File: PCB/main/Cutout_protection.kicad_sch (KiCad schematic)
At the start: 0 parts

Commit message: cutout
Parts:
- added D?: DIODE, symbol Simulation_SPICE:DIODE
- added D?: ZMM4V7-M, symbol Device:D_Zener
- added K?: ADW11, Relay_THT:Relay_1P1T_NO_10x24x18.8mm_Panasonic_ADW11xxxxW_THT, symbol Relay:ADW11
- added Q?: 2N3904, Package_TO_SOT_THT:TO-92_Inline, symbol Transistor_BJT:2N3904
- added R?: 150, symbol Device:R
- added R?: 1k, symbol Device:R
- added R?: 100k, symbol Device:R
- added U?: OPAMP, symbol pspice:OPAMP
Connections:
- net Battery_INP: now also D?.2 (K), K?.1, R?.1, R?.1, U?.4 (V+)
- net Relay_INP: now also K?.3
- net Relay_OUT: now also K?.5
- new net: D?.1 (A), K?.6, Q?.3 (C)
- new net: D?.1 (K), R?.2, U?.2 (-)
- new net: Q?.2 (B), U?.3
- new net: R?.1, R?.2, U?.1 (+)
- new net GND: D?.2 (A), Q?.1 (E), R?.2, U?.5 (V-)

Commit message: pmosfet name
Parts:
- gave numbers to parts that had none: 8
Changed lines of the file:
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@@
   (symbol (lib_id "Simulation_SPICE:DIODE") (at 130.81 93.98 90) (unit 1)
     (in_bom yes) (on_board yes) (fields_autoplaced)
-    (property "Reference" "D?" (id 0) (at 133.35 92.7099 90)
+    (property "Reference" "D5" (id 0) (at 133.35 92.7099 90)
       (effects (font (size 1.27 1.27)) (justify right))
     )
@@
   (symbol (lib_id "Device:R") (at 59.69 93.98 0) (unit 1)
     (in_bom yes) (on_board yes) (fields_autoplaced)
-    (property "Reference" "R?" (id 0) (at 62.23 92.7099 0)
+    (property "Reference" "R3" (id 0) (at 62.23 92.7099 0)
       (effects (font (size 1.27 1.27)) (justify left))
     )
@@
   (symbol (lib_id "Transistor_BJT:2N3904") (at 128.27 110.49 0) (unit 1)
     (in_bom yes) (on_board yes) (fields_autoplaced)
-    (property "Reference" "Q?" (id 0) (at 133.35 109.2199 0)
+    (property "Reference" "Q3" (id 0) (at 133.35 109.2199 0)
       (effects (font (size 1.27 1.27)) (justify left))
     )
@@
   (symbol (lib_id "power:GND") (at 54.61 127 0) (unit 1)
     (in_bom yes) (on_board yes) (fields_autoplaced)
-    (property "Reference" "#PWR?" (id 0) (at 54.61 133.35 0)
+    (property "Reference" "#PWR018" (id 0) (at 54.61 133.35 0)
       (effects (font (size 1.27 1.27)) hide)
     )
@@
   (symbol (lib_id "Device:R") (at 82.55 93.98 0) (unit 1)
     (in_bom yes) (on_board yes) (fields_autoplaced)
-    (property "Reference" "R?" (id 0) (at 85.09 92.7099 0)
+    (property "Reference" "R4" (id 0) (at 85.09 92.7099 0)
       (effects (font (size 1.27 1.27)) (justify left))
     )
@@
   (symbol (lib_id "Device:R") (at 82.55 111.76 0) (unit 1)
     (in_bom yes) (on_board yes) (fields_autoplaced)
-    (property "Reference" "R?" (id 0) (at 85.09 110.4899 0)
+    (property "Reference" "R5" (id 0) (at 85.09 110.4899 0)
       (effects (font (size 1.27 1.27)) (justify left))
     )
@@
   (symbol (lib_id "pspice:OPAMP") (at 106.68 101.6 0) (unit 1)
     (in_bom yes) (on_board yes) (fields_autoplaced)
-    (property "Reference" "U?" (id 0) (at 116.84 96.901 0))
+    (property "Reference" "U2" (id 0) (at 116.84 96.901 0))
     (property "Value" "OPAMP" (id 1) (at 116.84 99.441 0))
     (property "Footprint" "" (id 2) (at 106.68 101.6 0)
@@
   (symbol (lib_id "Relay:ADW11") (at 154.94 93.98 0) (unit 1)
     (in_bom yes) (on_board yes) (fields_autoplaced)
-    (property "Reference" "K?" (id 0) (at 166.37 92.7099 0)
+    (property "Reference" "K1" (id 0) (at 166.37 92.7099 0)
       (effects (font (size 1.27 1.27)) (justify left))
     )
@@
   (symbol (lib_id "Device:D_Zener") (at 59.69 111.76 270) (unit 1)
     (in_bom yes) (on_board yes) (fields_autoplaced)
-    (property "Reference" "D?" (id 0) (at 62.23 110.4899 90)
+    (property "Reference" "D4" (id 0) (at 62.23 110.4899 90)
       (effects (font (size 1.27 1.27)) (justify left))
     )

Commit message: Updated BOM
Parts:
- D4: footprint (none) -> Footprint_EEE3088F:LL-34_L3.5-W1.5-RD; JLC Part # (none) -> C707193; Price (none) -> 0.0159
- K1: JLC Part # (none) -> C34758; Price (none) -> 0.5145
- Q3: footprint Package_TO_SOT_THT:TO-92_Inline -> Package_TO_SOT_SMD:SOT-23; JLC Part # (none) -> C20526; Price (none) -> 0.0153
- R3: footprint (none) -> Resistor_SMD:R_0402_1005Metric; JLC Part # (none) -> C25082; Price (none) -> 0.0007
- R4: footprint (none) -> Resistor_SMD:R_0402_1005Metric; JLC Part # (none) -> C11702; Price (none) -> 0.0008
- R5: footprint (none) -> Resistor_SMD:R_0402_1005Metric; JLC Part # (none) -> C25744; Price (none) -> 0.0007
- U2: value OPAMP -> LM358DR2G; footprint (none) -> Package_SO:SOIC-8_3.9x4.9mm_P1.27mm; JLC Part # (none) -> C7950; Price (none) -> 0.149
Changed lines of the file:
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@@
       (effects (font (size 1.27 1.27)) (justify left))
     )
-    (property "Footprint" "" (id 2) (at 57.912 93.98 90)
+    (property "Footprint" "Resistor_SMD:R_0402_1005Metric" (id 2) (at 57.912 93.98 90)
       (effects (font (size 1.27 1.27)) hide)
     )
     (property "Datasheet" "~" (id 3) (at 59.69 93.98 0)
+      (effects (font (size 1.27 1.27)) hide)
+    )
+    (property "JLC Part #" "C25082" (id 4) (at 59.69 93.98 0)
+      (effects (font (size 1.27 1.27)) hide)
+    )
+    (property "Price" "0.0007" (id 5) (at 59.69 93.98 0)
       (effects (font (size 1.27 1.27)) hide)
     )
@@
       (effects (font (size 1.27 1.27)) (justify left))
     )
-    (property "Footprint" "Package_TO_SOT_THT:TO-92_Inline" (id 2) (at 133.35 112.395 0)
+    (property "Footprint" "Package_TO_SOT_SMD:SOT-23" (id 2) (at 133.35 112.395 0)
       (effects (font (size 1.27 1.27) italic) (justify left) hide)
     )
     (property "Datasheet" "https://www.onsemi.com/pub/Collateral/2N3903-D.PDF" (id 3) (at 128.27 110.49 0)
       (effects (font (size 1.27 1.27)) (justify left) hide)
+    )
+    (property "JLC Part #" "C20526" (id 4) (at 128.27 110.49 0)
+      (effects (font (size 1.27 1.27)) hide)
+    )
+    (property "Price" "0.0153" (id 5) (at 128.27 110.49 0)
+      (effects (font (size 1.27 1.27)) hide)
     )
     (pin "1")
@@
       (effects (font (size 1.27 1.27)) (justify left))
     )
-    (property "Footprint" "" (id 2) (at 80.772 93.98 90)
+    (property "Footprint" "Resistor_SMD:R_0402_1005Metric" (id 2) (at 80.772 93.98 90)
       (effects (font (size 1.27 1.27)) hide)
     )
     (property "Datasheet" "~" (id 3) (at 82.55 93.98 0)
+      (effects (font (size 1.27 1.27)) hide)
+    )
+    (property "JLC Part #" "C11702" (id 4) (at 82.55 93.98 0)
+      (effects (font (size 1.27 1.27)) hide)
+    )
+    (property "Price" "0.0008" (id 5) (at 82.55 93.98 0)
       (effects (font (size 1.27 1.27)) hide)
     )
@@
       (effects (font (size 1.27 1.27)) (justify left))
     )
-    (property "Footprint" "" (id 2) (at 80.772 111.76 90)
+    (property "Footprint" "Resistor_SMD:R_0402_1005Metric" (id 2) (at 80.772 111.76 90)
       (effects (font (size 1.27 1.27)) hide)
     )
     (property "Datasheet" "~" (id 3) (at 82.55 111.76 0)
+      (effects (font (size 1.27 1.27)) hide)
+    )
+    (property "JLC Part #" "C25744" (id 4) (at 82.55 111.76 0)
+      (effects (font (size 1.27 1.27)) hide)
+    )
+    (property "Price" "0.0007" (id 5) (at 82.55 111.76 0)
       (effects (font (size 1.27 1.27)) hide)
     )
@@
     (in_bom yes) (on_board yes) (fields_autoplaced)
     (property "Reference" "U2" (id 0) (at 116.84 96.901 0))
-    (property "Value" "OPAMP" (id 1) (at 116.84 99.441 0))
-    (property "Footprint" "" (id 2) (at 106.68 101.6 0)
+    (property "Value" "LM358DR2G" (id 1) (at 116.84 99.441 0))
+    (property "Footprint" "Package_SO:SOIC-8_3.9x4.9mm_P1.27mm" (id 2) (at 106.68 101.6 0)
       (effects (font (size 1.27 1.27)) hide)
     )
     (property "Datasheet" "~" (id 3) (at 106.68 101.6 0)
+      (effects (font (size 1.27 1.27)) hide)
+    )
+    (property "JLC Part #" "C7950" (id 4) (at 106.68 101.6 0)
+      (effects (font (size 1.27 1.27)) hide)
+    )
+    (property "Price" "0.149" (id 5) (at 106.68 101.6 0)
       (effects (font (size 1.27 1.27)) hide)
     )
@@
       (effects (font (size 1.27 1.27)) hide)
     )
+    (property "JLC Part #" "C34758" (id 4) (at 154.94 93.98 0)
+      (effects (font (size 1.27 1.27)) hide)
+    )
+    (property "Price" "0.5145" (id 5) (at 154.94 93.98 0)
+      (effects (font (size 1.27 1.27)) hide)
+    )
     (pin "1")
     (pin "3")
@@
       (effects (font (size 1.27 1.27)) (justify left))
     )
-    (property "Footprint" "" (id 2) (at 59.69 111.76 0)
+    (property "Footprint" "Footprint_EEE3088F:LL-34_L3.5-W1.5-RD" (id 2) (at 59.69 111.76 0)
       (effects (font (size 1.27 1.27)) hide)
     )
@@
       (effects (font (size 1.27 1.27)) hide)
     )
+    (property "JLC Part #" "C707193" (id 4) (at 59.69 111.76 0)
+      (effects (font (size 1.27 1.27)) hide)
+    )
+    (property "Price" "0.0159" (id 5) (at 59.69 111.76 0)
+      (effects (font (size 1.27 1.27)) hide)
+    )

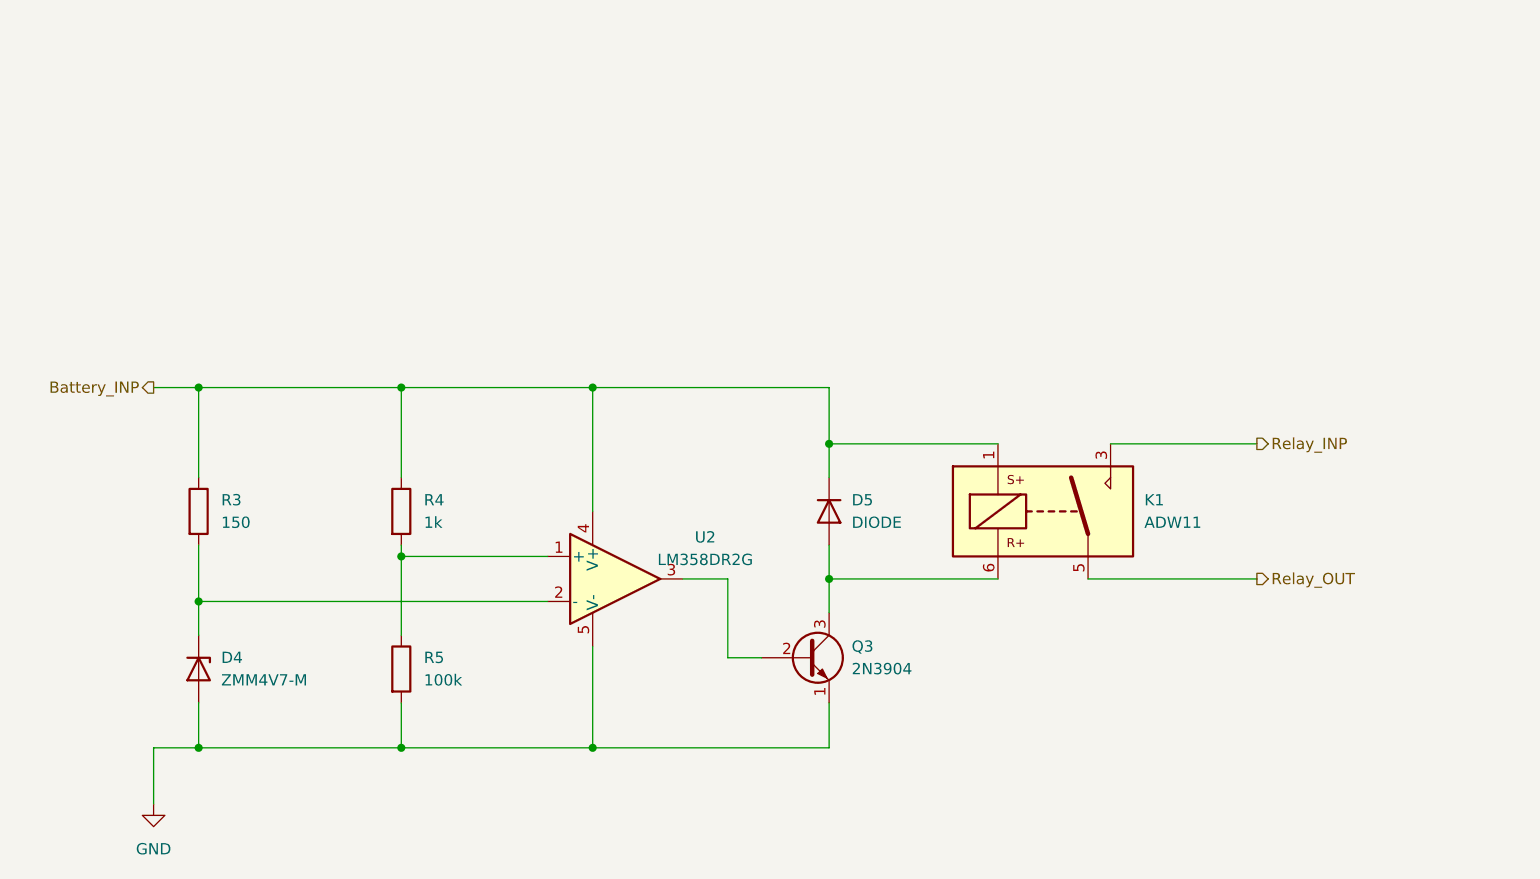
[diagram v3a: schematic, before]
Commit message: Add footprints and test points
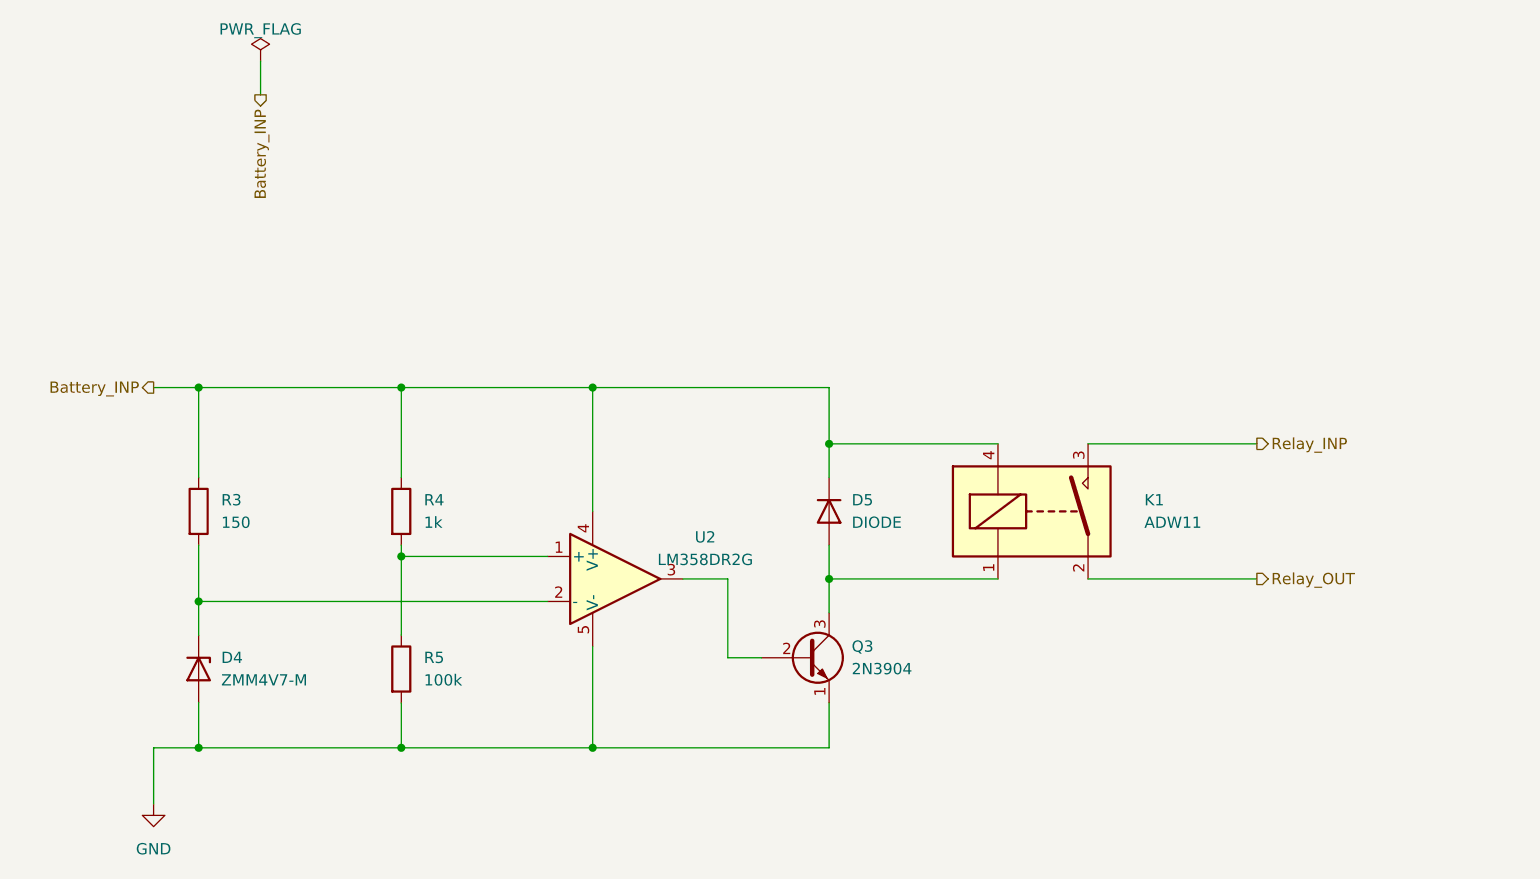
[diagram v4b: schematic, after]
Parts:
- D5: footprint (none) -> Footprint_EEE3088F:DO-214AC_L4.3-W2.7-LS5.3-RD; JLC Part # (none) -> C95872; Price (none) -> 0.0089
- K1: footprint Relay_THT:Relay_1P1T_NO_10x24x18.8mm_Panasonic_ADW11xxxxW_THT -> Relay_THT:Relay_SPST_Omron-G5Q-1A; symbol Relay:ADW11 -> Symbol_EEE3088F:G5NB
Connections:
- net Battery_INP: now also K1.4; no longer K1.1
- net Relay_OUT: now also K1.2; no longer K1.5
- net at D5.1 (A), Q3.3 (C): now also K1.1; no longer K1.6
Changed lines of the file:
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@@
+    (stroke (width 0) (type default) (color 0 0 0 0))
+  )
+  (wire (pts (xy 66.675 43.18) (xy 66.675 46.99))
     (stroke (width 0) (type default) (color 0 0 0 0))
   )
@@
     (stroke (width 0) (type default) (color 0 0 0 0))
   )
-  (wire (pts (xy 162.56 86.36) (xy 179.07 86.36))
+  (wire (pts (xy 160.02 86.36) (xy 179.07 86.36))
     (stroke (width 0) (type default) (color 0 0 0 0))
   )
@@
     (effects (font (size 1.27 1.27)) (justify left))
   )
+  (hierarchical_label "Battery_INP" (shape output) (at 66.675 46.99 270)
+    (effects (font (size 1.27 1.27)) (justify right))
+  )
   (symbol (lib_id "Simulation_SPICE:DIODE") (at 130.81 93.98 90) (unit 1)
     (in_bom yes) (on_board yes) (fields_autoplaced)
@@
       (effects (font (size 1.27 1.27)) (justify right))
     )
-    (property "Footprint" "" (id 2) (at 130.81 93.98 0)
+    (property "Footprint" "Footprint_EEE3088F:DO-214AC_L4.3-W2.7-LS5.3-RD" (id 2) (at 130.81 93.98 0)
       (effects (font (size 1.27 1.27)) hide)
     )
@@
     (property "Spice_Primitive" "D" (id 5) (at 130.81 93.98 0)
       (effects (font (size 1.27 1.27)) (justify left) hide)
+    )
+    (property "JLC Part #" "C95872" (id 6) (at 130.81 93.98 0)
+      (effects (font (size 1.27 1.27)) hide)
+    )
+    (property "Price" "0.0089" (id 7) (at 130.81 93.98 0)
+      (effects (font (size 1.27 1.27)) hide)
     )
     (pin "1")
@@
     (pin "5")
   )
-  (symbol (lib_id "Relay:ADW11") (at 154.94 93.98 0) (unit 1)
+  (symbol (lib_id "power:PWR_FLAG") (at 66.675 43.18 0) (unit 1)
+    (in_bom yes) (on_board yes) (fields_autoplaced)
+    (property "Reference" "#FLG0102" (id 0) (at 66.675 41.275 0)
+      (effects (font (size 1.27 1.27)) hide)
+    )
+    (property "Value" "PWR_FLAG" (id 1) (at 66.675 39.6042 0))
+    (property "Footprint" "" (id 2) (at 66.675 43.18 0)
+      (effects (font (size 1.27 1.27)) hide)
+    )
+    (property "Datasheet" "~" (id 3) (at 66.675 43.18 0)
+      (effects (font (size 1.27 1.27)) hide)
+    )
+    (pin "1")
+  )
+  (symbol (lib_id "Symbol_EEE3088F:G5NB") (at 154.94 93.98 0) (unit 1)
     (in_bom yes) (on_board yes) (fields_autoplaced)
     (property "Reference" "K1" (id 0) (at 166.37 92.7099 0)
@@
       (effects (font (size 1.27 1.27)) (justify left))
     )
-    (property "Footprint" "Relay_THT:Relay_1P1T_NO_10x24x18.8mm_Panasonic_ADW11xxxxW_THT" (id 2) (at 188.595 95.25 0)
-      (effects (font (size 1.27 1.27)) hide)
-    )
-    (property "Datasheet" "https://www.panasonic-electric-works.com/pew/es/downloads/ds_dw_hl_en.pdf" (id 3) (at 154.94 93.98 0)
+    (property "Footprint" "Relay_THT:Relay_SPST_Omron-G5Q-1A" (id 2) (at 163.83 95.25 0)
+      (effects (font (size 1.27 1.27)) (justify left) hide)
+    )
+    (property "Datasheet" "https://www.omron.com/ecb/products/pdf/en-g5q.pdf" (id 3) (at 154.94 93.98 0)
       (effects (font (size 1.27 1.27)) hide)
     )
@@
     )
     (pin "1")
+    (pin "2")
     (pin "3")
-    (pin "5")
-    (pin "6")
+    (pin "4")
   )
   (symbol (lib_id "Device:D_Zener") (at 59.69 111.76 270) (unit 1)

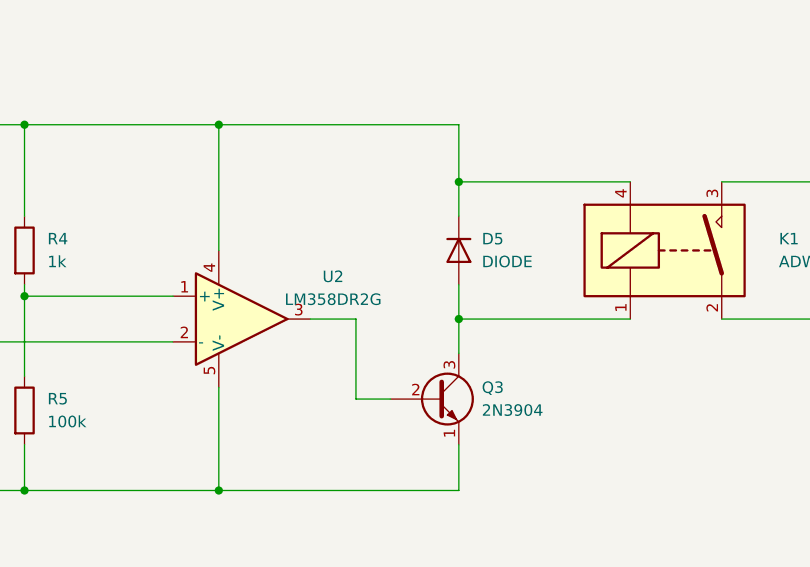
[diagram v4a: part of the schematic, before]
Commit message: Correct op-amp symbol
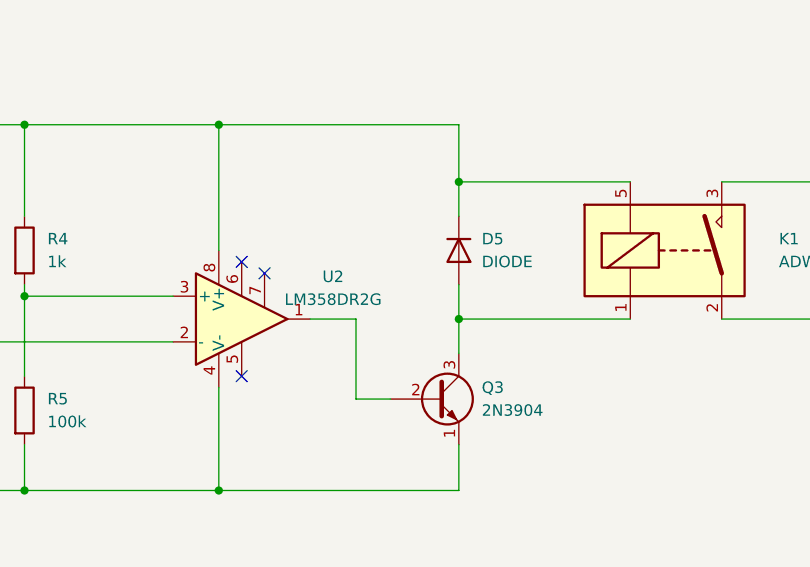
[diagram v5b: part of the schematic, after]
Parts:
- K1: symbol Symbol_EEE3088F:G5NB -> Relay:G5Q-1A
- U2: symbol pspice:OPAMP -> Symbol_EEE3088F:LM358DR2G
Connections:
- net Battery_INP: now also K1.5, U2.8 (V+); no longer K1.4, U2.4 (V+)
- net GND: now also U2.4 (V-); no longer U2.5 (V-)
- net at Q3.2 (B): now also U2.1; no longer U2.3
- net at R4.2, R5.1: now also U2.3 (+); no longer U2.1 (+)
- no-connect marks 0 -> 3
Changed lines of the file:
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@@
   (junction (at 104.14 120.65) (diameter 0) (color 0 0 0 0)
   )
+  (no_connect (at 106.68 107.95))
+  (no_connect (at 106.68 95.25))
+  (no_connect (at 109.22 96.52))
   (wire (pts (xy 104.14 80.01) (xy 82.55 80.01))
     (stroke (width 0) (type default) (color 0 0 0 0))
@@
     (pin "2")
   )
-  (symbol (lib_id "pspice:OPAMP") (at 106.68 101.6 0) (unit 1)
+  (symbol (lib_id "Symbol_EEE3088F:LM358DR2G") (at 106.68 101.6 0) (unit 1)
     (in_bom yes) (on_board yes) (fields_autoplaced)
     (property "Reference" "U2" (id 0) (at 116.84 96.901 0))
@@
     (pin "4")
     (pin "5")
+    (pin "6")
+    (pin "7")
+    (pin "8")
   )
   (symbol (lib_id "power:PWR_FLAG") (at 66.675 43.18 0) (unit 1)
@@
     (pin "1")
   )
-  (symbol (lib_id "Symbol_EEE3088F:G5NB") (at 154.94 93.98 0) (unit 1)
+  (symbol (lib_id "Relay:G5Q-1A") (at 154.94 93.98 0) (unit 1)
     (in_bom yes) (on_board yes) (fields_autoplaced)
     (property "Reference" "K1" (id 0) (at 166.37 92.7099 0)
@@
     (pin "2")
     (pin "3")
-    (pin "4")
+    (pin "5")
   )
   (symbol (lib_id "Device:D_Zener") (at 59.69 111.76 270) (unit 1)
